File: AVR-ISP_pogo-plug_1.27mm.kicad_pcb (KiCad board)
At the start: 2 copper layers, 16.3 x 11.3 mm, 6 parts, among them P1 CONN_6, P2 CONN_6

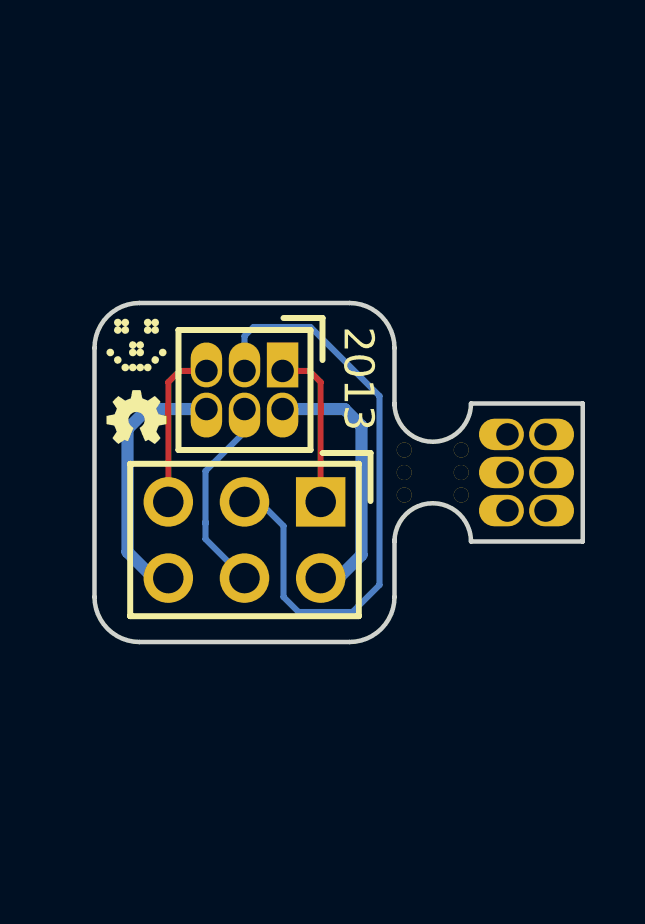
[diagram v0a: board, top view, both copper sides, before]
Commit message: Changed some traces. Don't connect to pads next to drills.
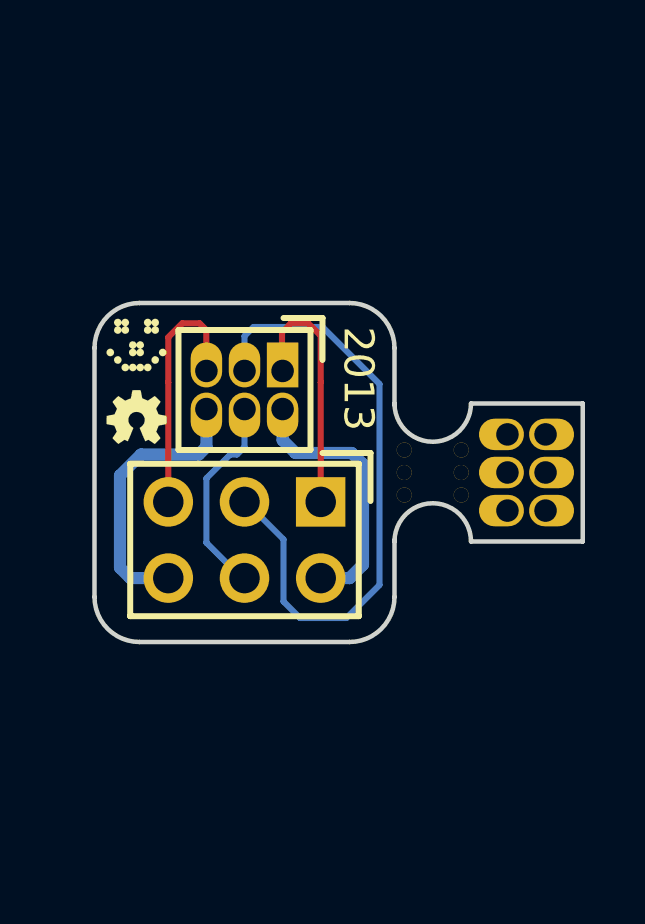
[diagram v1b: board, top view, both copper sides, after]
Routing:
- net /MISO: track 5.42 -> 8.42 mm
- net /RESET: track 5.42 -> 8.41 mm
- net /GND: track 8.73 -> 9.85 mm
- net /MOSI: track 6.78 -> 7.64 mm
- net /V-target: track 8.84 -> 9.58 mm
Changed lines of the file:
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@@
-(kicad_pcb (version 3) (host pcbnew "(2013-07-03 BZR 4236)-testing")
+(kicad_pcb (version 3) (host pcbnew "(2013-09-01 BZR 4308)-product")
   (general
     (links 6)
@@
     (thickness 1.6)
     (drawings 15)
-    (tracks 33)
+    (tracks 48)
     (zones 0)
     (modules 6)
@@
     (pad_to_mask_clearance 0)
     (aux_axis_origin 0 0)
-    (visible_elements FFFFFF7F)
+    (visible_elements FFFFFF61)
     (pcbplotparams
       (layerselection 284196865)
@@
     (effects (font (size 1 1) (thickness 0.25)))
   )
-  (segment (start 64.7 78.6) (end 65.57 79.47) (width 0.4064) (layer B.Cu) (net 1))
-  (segment (start 65.365 73.835) (end 64.7 74.5) (width 0.4064) (layer B.Cu) (net 1))
-  (segment (start 64.7 74.5) (end 64.7 78.6) (width 0.4064) (layer B.Cu) (net 1))
-  (segment (start 67.33 73.835) (end 65.365 73.835) (width 0.4064) (layer B.Cu) (net 1))
+  (segment (start 66.06 79.47) (end 64.795 79.47) (width 0.4064) (layer B.Cu) (net 1))
+  (segment (start 67.33 75.095) (end 67.33 73.835) (width 0.4064) (layer B.Cu) (net 1))
+  (segment (start 67.075 75.35) (end 67.33 75.095) (width 0.4064) (layer B.Cu) (net 1))
+  (segment (start 65.15 75.35) (end 67.075 75.35) (width 0.4064) (layer B.Cu) (net 1))
+  (segment (start 64.45 76.05) (end 65.15 75.35) (width 0.4064) (layer B.Cu) (net 1))
+  (segment (start 64.45 79.125) (end 64.45 76.05) (width 0.4064) (layer B.Cu) (net 1))
+  (segment (start 64.795 79.47) (end 64.45 79.125) (width 0.4064) (layer B.Cu) (net 1))
   (segment (start 65.57 79.47) (end 66.06 79.47) (width 0.4064) (layer B.Cu) (net 1))
-  (segment (start 69.87 72.565) (end 70.765 72.565) (width 0.2032) (layer F.Cu) (net 2))
-  (segment (start 70.765 72.565) (end 71.14 72.94) (width 0.2032) (layer F.Cu) (net 2))
-  (segment (start 71.14 72.94) (end 71.14 76.93) (width 0.2032) (layer F.Cu) (net 2) (status 20))
-  (segment (start 67.3 77.6) (end 67.3 78.17) (width 0.2032) (layer B.Cu) (net 3))
-  (segment (start 67.3 78.17) (end 68.6 79.47) (width 0.2032) (layer B.Cu) (net 3))
+  (segment (start 71.14 72.94) (end 71.14 71.39) (width 0.2032) (layer F.Cu) (net 2))
+  (segment (start 71.14 76.93) (end 71.14 72.94) (width 0.2032) (layer F.Cu) (net 2) (status 20))
+  (segment (start 69.85 72.545) (end 69.87 72.565) (width 0.2032) (layer F.Cu) (net 2))
+  (segment (start 69.85 71.275) (end 69.85 72.545) (width 0.2032) (layer F.Cu) (net 2))
+  (segment (start 70.15 70.975) (end 69.85 71.275) (width 0.2032) (layer F.Cu) (net 2))
+  (segment (start 70.725 70.975) (end 70.15 70.975) (width 0.2032) (layer F.Cu) (net 2))
+  (segment (start 71.14 71.39) (end 70.725 70.975) (width 0.2032) (layer F.Cu) (net 2))
+  (segment (start 68.6 79.47) (end 68.51 79.47) (width 0.2032) (layer B.Cu) (net 3) (status C00000))
+  (segment (start 68.125 75.35) (end 68.35 75.35) (width 0.2032) (layer B.Cu) (net 3))
+  (segment (start 68.35 75.35) (end 68.6 75.1) (width 0.2032) (layer B.Cu) (net 3))
+  (segment (start 68.6 75.1) (end 68.6 73.835) (width 0.2032) (layer B.Cu) (net 3))
+  (segment (start 67.33 76.145) (end 68.125 75.35) (width 0.2032) (layer B.Cu) (net 3))
+  (segment (start 67.33 78.29) (end 67.33 76.145) (width 0.2032) (layer B.Cu) (net 3))
+  (segment (start 68.51 79.47) (end 67.33 78.29) (width 0.2032) (layer B.Cu) (net 3) (status 400000))
   (segment (start 68.6 73.835) (end 68.6 74.6) (width 0.2032) (layer B.Cu) (net 3))
-  (segment (start 68.6 74.6) (end 67.3 75.9) (width 0.2032) (layer B.Cu) (net 3))
-  (segment (start 67.3 75.9) (end 67.3 77.6) (width 0.2032) (layer B.Cu) (net 3))
-  (segment (start 67.3 77.6) (end 67.3 77.67) (width 0.2032) (layer B.Cu) (net 3))
-  (segment (start 67.33 72.565) (end 66.435 72.565) (width 0.2032) (layer F.Cu) (net 4))
-  (segment (start 66.435 72.565) (end 66.06 72.94) (width 0.2032) (layer F.Cu) (net 4))
-  (segment (start 66.06 72.94) (end 66.06 76.93) (width 0.2032) (layer F.Cu) (net 4) (status 20))
-  (segment (start 69.9 77.73) (end 69.1 76.93) (width 0.2032) (layer B.Cu) (net 5))
-  (segment (start 69.9 80.1) (end 69.9 77.73) (width 0.2032) (layer B.Cu) (net 5))
-  (segment (start 70.4 80.6) (end 69.9 80.1) (width 0.2032) (layer B.Cu) (net 5))
-  (segment (start 72.2 80.6) (end 70.4 80.6) (width 0.2032) (layer B.Cu) (net 5))
-  (segment (start 73.1 79.7) (end 72.2 80.6) (width 0.2032) (layer B.Cu) (net 5))
-  (segment (start 73.1 73.4) (end 73.1 79.7) (width 0.2032) (layer B.Cu) (net 5))
-  (segment (start 70.8 71.1) (end 73.1 73.4) (width 0.2032) (layer B.Cu) (net 5))
-  (segment (start 68.9 71.1) (end 70.8 71.1) (width 0.2032) (layer B.Cu) (net 5))
+  (segment (start 66.06 72.94) (end 66.06 71.44) (width 0.2032) (layer F.Cu) (net 4))
+  (segment (start 66.06 76.93) (end 66.06 72.94) (width 0.2032) (layer F.Cu) (net 4) (status 20))
+  (segment (start 67.33 71.205) (end 67.33 72.565) (width 0.2032) (layer F.Cu) (net 4))
+  (segment (start 67.1 70.975) (end 67.33 71.205) (width 0.2032) (layer F.Cu) (net 4))
+  (segment (start 66.525 70.975) (end 67.1 70.975) (width 0.2032) (layer F.Cu) (net 4))
+  (segment (start 66.06 71.44) (end 66.525 70.975) (width 0.2032) (layer F.Cu) (net 4))
+  (segment (start 69.9 78.18) (end 68.65 76.93) (width 0.2032) (layer B.Cu) (net 5))
+  (segment (start 69.9 80.25) (end 69.9 78.18) (width 0.2032) (layer B.Cu) (net 5))
+  (segment (start 70.45 80.8) (end 69.9 80.25) (width 0.2032) (layer B.Cu) (net 5))
+  (segment (start 72 80.8) (end 70.45 80.8) (width 0.2032) (layer B.Cu) (net 5))
+  (segment (start 73.1 79.7) (end 72 80.8) (width 0.2032) (layer B.Cu) (net 5))
+  (segment (start 73.1 73) (end 73.1 79.7) (width 0.2032) (layer B.Cu) (net 5))
+  (segment (start 71.2 71.1) (end 73.1 73) (width 0.2032) (layer B.Cu) (net 5))
+  (segment (start 68.9 71.1) (end 71.2 71.1) (width 0.2032) (layer B.Cu) (net 5))
   (segment (start 68.6 71.4) (end 68.9 71.1) (width 0.2032) (layer B.Cu) (net 5))
   (segment (start 68.6 72.565) (end 68.6 71.4) (width 0.2032) (layer B.Cu) (net 5))
-  (segment (start 69.1 76.93) (end 68.6 76.93) (width 0.2032) (layer B.Cu) (net 5))
-  (segment (start 72.5 78.7) (end 71.73 79.47) (width 0.4064) (layer B.Cu) (net 6))
-  (segment (start 71.935 73.835) (end 72.5 74.4) (width 0.4064) (layer B.Cu) (net 6))
-  (segment (start 72.5 74.4) (end 72.5 78.7) (width 0.4064) (layer B.Cu) (net 6))
-  (segment (start 69.87 73.835) (end 71.935 73.835) (width 0.4064) (layer B.Cu) (net 6))
+  (segment (start 68.65 76.93) (end 68.6 76.93) (width 0.2032) (layer B.Cu) (net 5) (status 800000))
+  (segment (start 71.14 79.47) (end 72.105 79.47) (width 0.4064) (layer B.Cu) (net 6))
+  (segment (start 69.87 74.87) (end 69.87 73.835) (width 0.4064) (layer B.Cu) (net 6))
+  (segment (start 70.3 75.3) (end 69.87 74.87) (width 0.4064) (layer B.Cu) (net 6))
+  (segment (start 72.175 75.3) (end 70.3 75.3) (width 0.4064) (layer B.Cu) (net 6))
+  (segment (start 72.55 75.675) (end 72.175 75.3) (width 0.4064) (layer B.Cu) (net 6))
+  (segment (start 72.55 79.025) (end 72.55 75.675) (width 0.4064) (layer B.Cu) (net 6))
+  (segment (start 72.105 79.47) (end 72.55 79.025) (width 0.4064) (layer B.Cu) (net 6))
   (segment (start 71.73 79.47) (end 71.14 79.47) (width 0.4064) (layer B.Cu) (net 6))
 )

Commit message: Added sub-boards to triple board thickness for better  pogo-pin alignment.
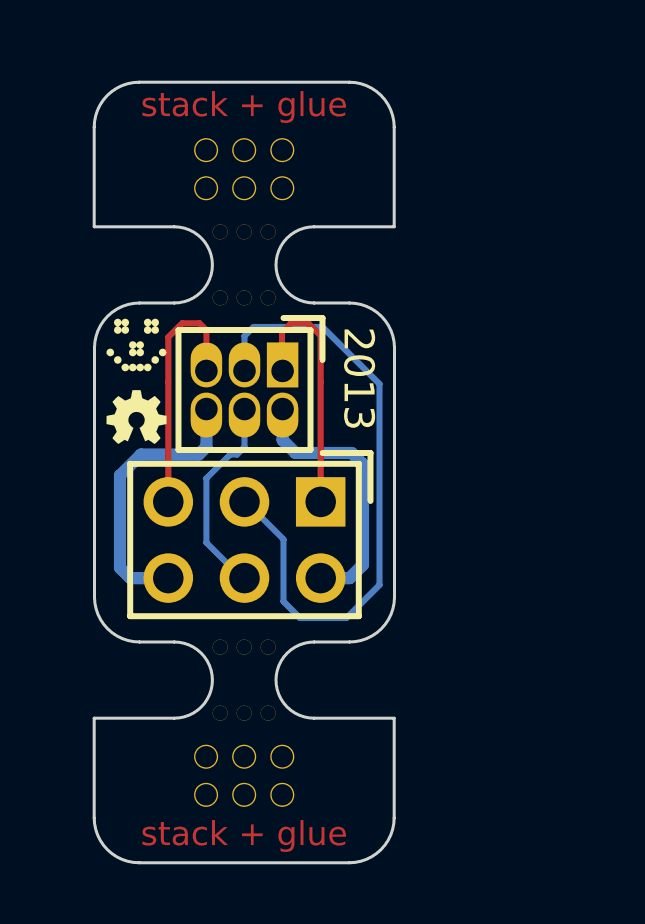
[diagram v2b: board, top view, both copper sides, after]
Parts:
- removed P?: VAL**, MADW__PIN_ARRAY_3x2_1.27mm
- removed mouse-bite-2mm: VAL**, MADW__mouse-bite-2mm-slot
- added P2: CONN_6, MADW__PIN_ARRAY_3x2_1.27mm, F.Cu at (68.6, 86.1)
- added P2: CONN_6, MADW__PIN_ARRAY_3x2_1.27mm, F.Cu at (68.6, 65.8)
- added mouse-bite-2.54mm-slot: VAL**, MADW__mouse-bite-2.54mm-slot, F.Cu at (68.6, 69.0)
- added mouse-bite-2.54mm-slot: VAL**, MADW__mouse-bite-2.54mm-slot, F.Cu at (68.6, 82.9)
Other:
- board size 16.3 x 11.3 mm -> 10 x 26 mm
- board text added: "stack + glue"

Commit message: Drill-size issues again...
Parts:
- added 1PIN: P***, 1pin, B.Cu at (65.1, 86.1)
- added 1PIN: P***, 1pin, F.Cu at (72.1, 65.8)
- added 1PIN: P***, 1pin, B.Cu at (72.1, 86.1)
- added 1PIN: P***, 1pin, B.Cu at (65.1, 65.8)
- added 1PIN: P***, 1pin, B.Cu at (72.1, 65.8)
- added 1PIN: P***, 1pin, B.Cu at (65.1, 73.2)
- added 1PIN: P***, 1pin, B.Cu at (72.1, 73.2)
- added 1PIN: P***, 1pin, F.Cu at (65.1, 86.1)
- added 1PIN: P***, 1pin, F.Cu at (72.1, 86.1)
- added 1PIN: P***, 1pin, F.Cu at (65.1, 65.8)
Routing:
- net /SCK: track 21.0 -> 22.1 mm

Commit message: Revert "Drill-size issues again..."
This reverts commit 78704ad755869ccbc9e371843dd45850562db76e.
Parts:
- removed 1PIN (x10): P***, 1pin
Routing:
- net /SCK: track 22.1 -> 21.0 mm

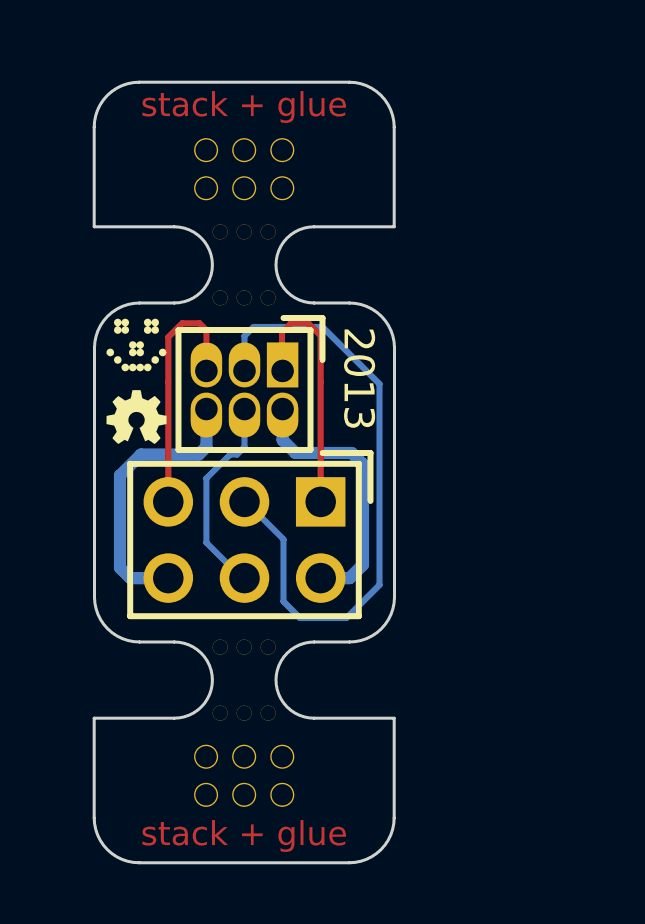
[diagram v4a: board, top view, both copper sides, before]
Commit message: Revert "Added sub-boards to triple board thickness for better  pogo-pin alignment."
This reverts commit 808a31bfee8c9cebc64c52d68362d3861d50fe81.
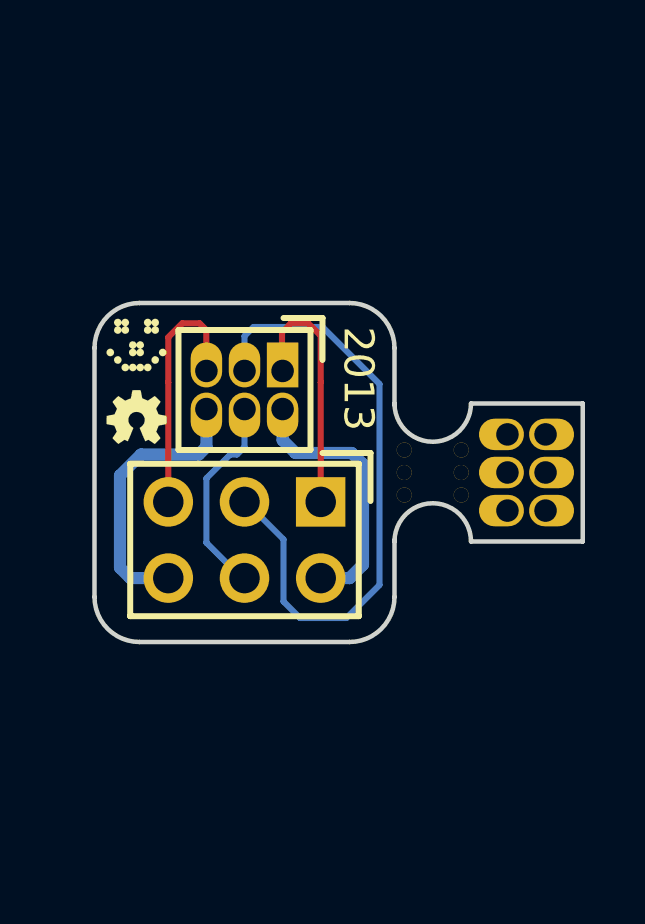
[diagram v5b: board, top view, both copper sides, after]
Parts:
- removed the P2 at (68.6, 86.1)
- removed the P2 at (68.6, 65.8)
- removed mouse-bite-2.54mm-slot (x2): VAL**, MADW__mouse-bite-2.54mm-slot
- added P?: VAL**, MADW__PIN_ARRAY_3x2_1.27mm, F.Cu at (78.0, 76.0)
- added mouse-bite-2mm: VAL**, MADW__mouse-bite-2mm-slot, F.Cu at (74.9, 76.0)
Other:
- board size 10 x 26 mm -> 16.3 x 11.3 mm
- board text removed: "stack + glue"

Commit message: New idea how to assemble the pogo-pins.
* one sub-board is an 'align tool' with small drills,
  so the heads can register with them.

* the other's holes are large enough for the pins'
  shafts. This should stabilize the pins sideways.
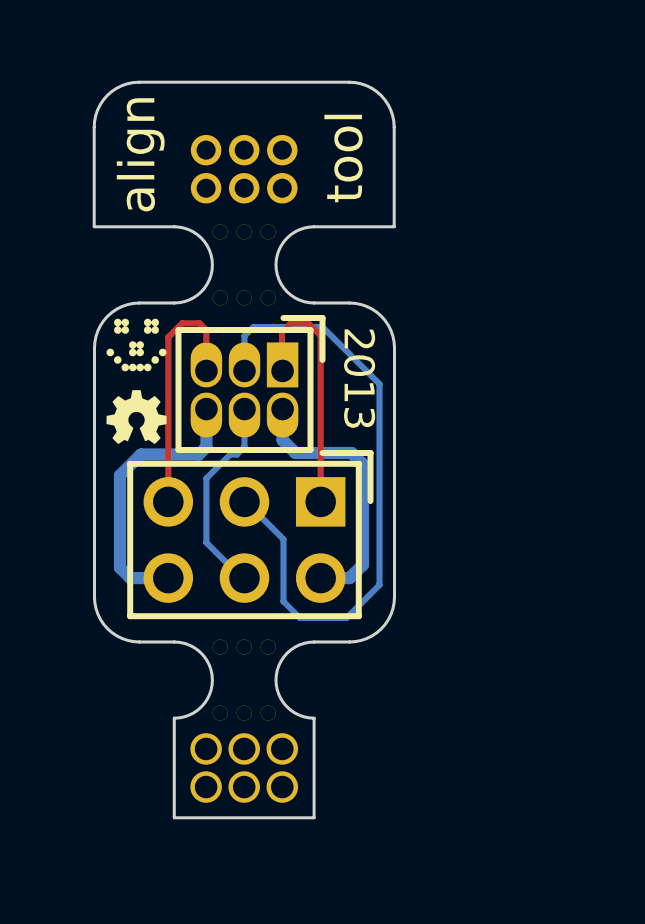
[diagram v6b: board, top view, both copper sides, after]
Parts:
- removed P?: VAL**, MADW__PIN_ARRAY_3x2_1.27mm
- removed mouse-bite-2mm: VAL**, MADW__mouse-bite-2mm-slot
- added P3: CONN_6, MADW__PIN_ARRAY_3x2_1.27mm, F.Cu at (68.6, 65.8)
- added P4: CONN_6, MADW__PIN_ARRAY_3x2_1.27mm, F.Cu at (68.6, 85.8)
- added mouse-bite-2.54mm-slot: VAL**, MADW__mouse-bite-2.54mm-slot, F.Cu at (68.6, 69.0)
- added mouse-bite-2.54mm-slot: VAL**, MADW__mouse-bite-2.54mm-slot, F.Cu at (68.6, 82.9)
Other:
- board size 16.3 x 11.3 mm -> 10 x 24.5 mm
- board text added: "align"
- board text added: "tool"

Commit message: Experimenting with yet another scheme (0.6mm PCBs).
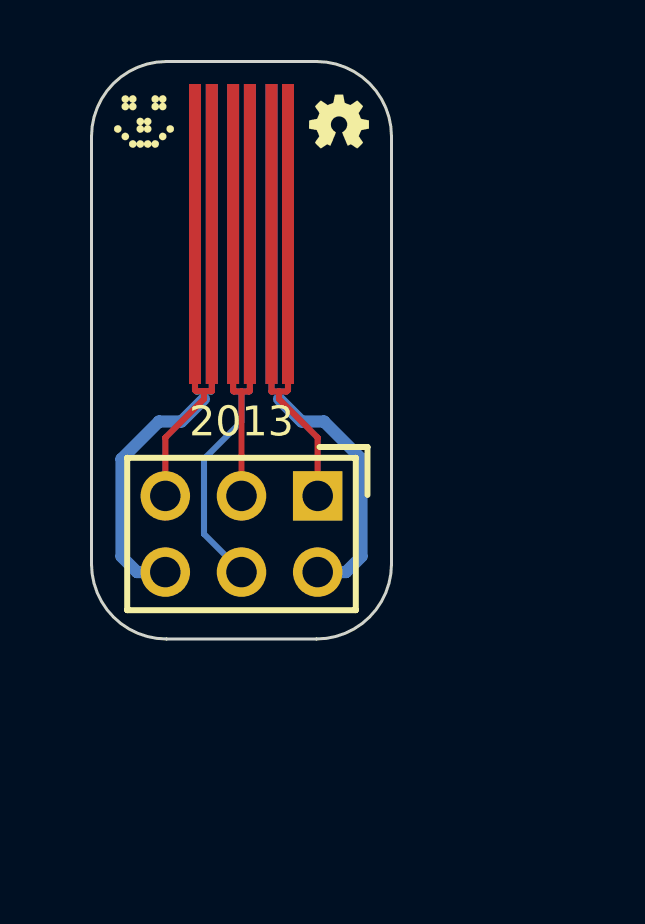
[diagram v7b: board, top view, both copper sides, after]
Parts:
- removed P3, P4: CONN_6, MADW__PIN_ARRAY_3x2_1.27mm
- removed mouse-bite-2.54mm-slot (x2): VAL**, MADW__mouse-bite-2.54mm-slot
- moved G2 11.9 mm to (71.8, 64.2)
- moved G1 7.45 mm to (65.2, 64.2)
- moved P2 5.20 mm to (68.5, 68.0), turned to 0 degrees
- moved P1 0.22 mm to (68.5, 78.0)
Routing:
- net /MOSI: track 7.64 -> 18.1 mm
- net /V-target: track 9.58 -> 19.8 mm
- net /GND: track 9.85 -> 19.8 mm
- net /RESET: track 8.41 -> 15.0 mm
- net /MISO: track 8.42 -> 15.0 mm
- net /SCK: track 21.0 -> 14.5 mm
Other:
- board size 10 x 24.5 mm -> 10 x 19.2 mm
- board text removed: "align"
- board text removed: "tool"
